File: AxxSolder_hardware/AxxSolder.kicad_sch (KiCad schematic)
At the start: 152 parts, among them IC1 TLV76733DRVR, IC2 OPA2387DSGT, IC3 LMR54406DBVR, IC4 STM32G431CBT6, IC5 TPD4E1U06DBVR, IC6 STUSB4500QTR, IC7 MAX16171ATA_VY+T, IC8 LTC4440AHMS8E, IC9 INA281A5QDBVRQ1, J1 USB4110-GF-A, J2 691243110009, J3 TSW-102-07-T-S, J4 61300611821, J5 TSW-102-07-T-S, J6 TSW-102-07-T-S, J7 TSW-108-07-T-S, J8 Conn_01x01_Pin, Q1 STL9P3LLH6, Q2 STL10N3LLH5, Q3 2N7002NXAKR, U2 PEC11J-9215F-S0015, U3 BSC014N04LS

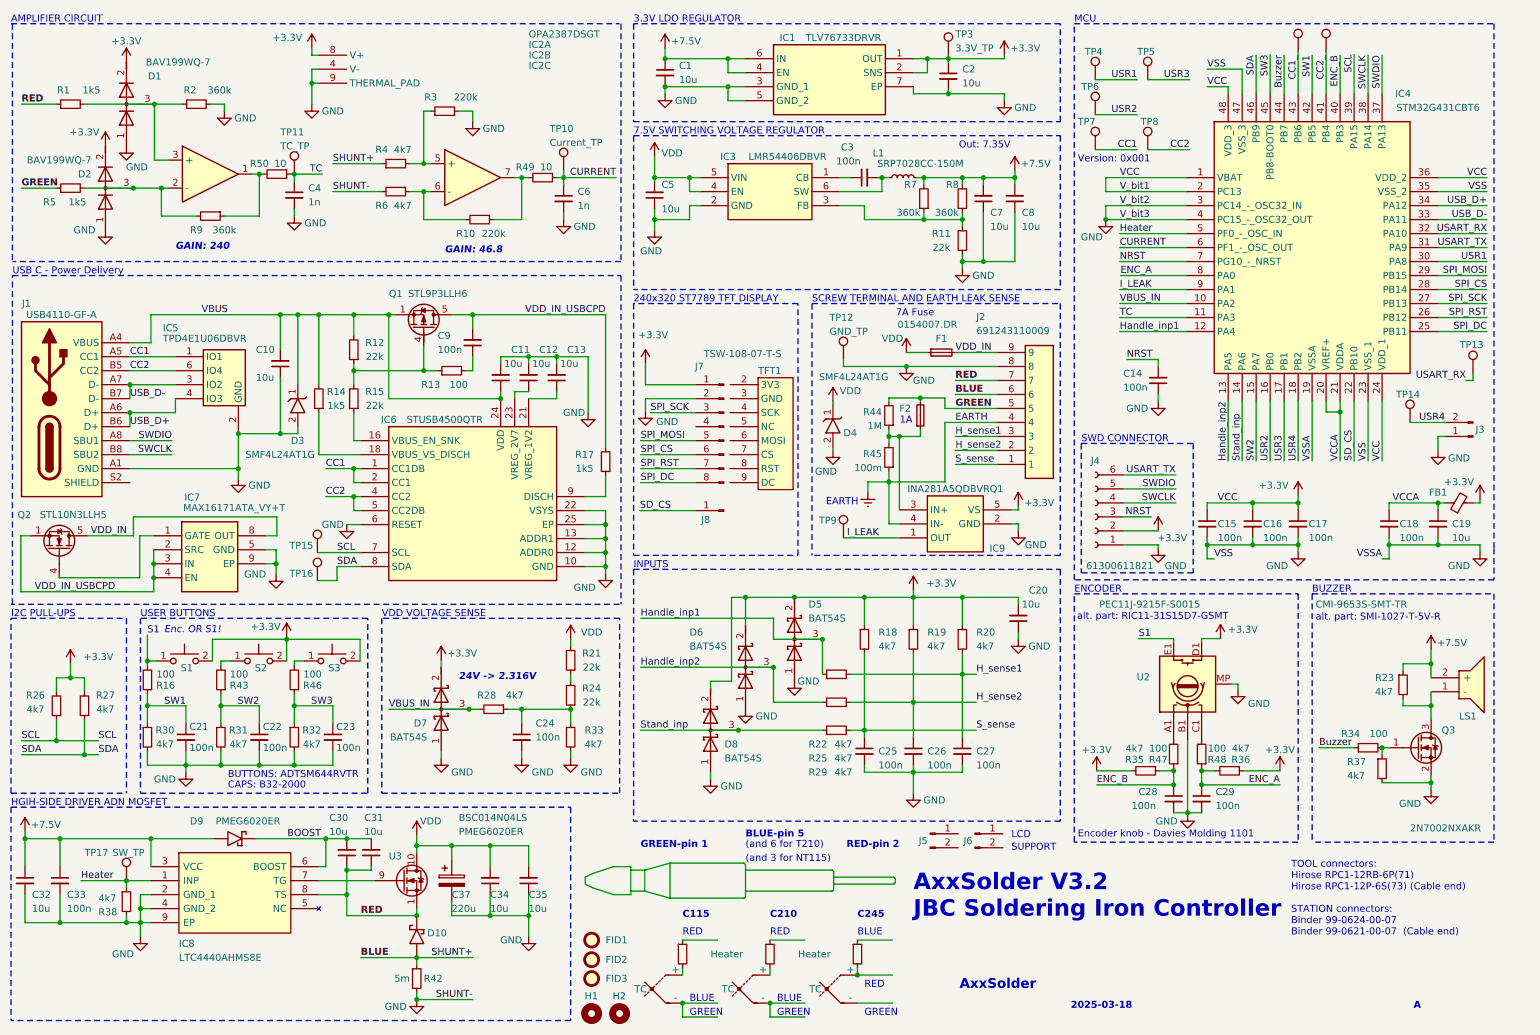
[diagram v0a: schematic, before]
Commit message: added pwr connections for relay add on board
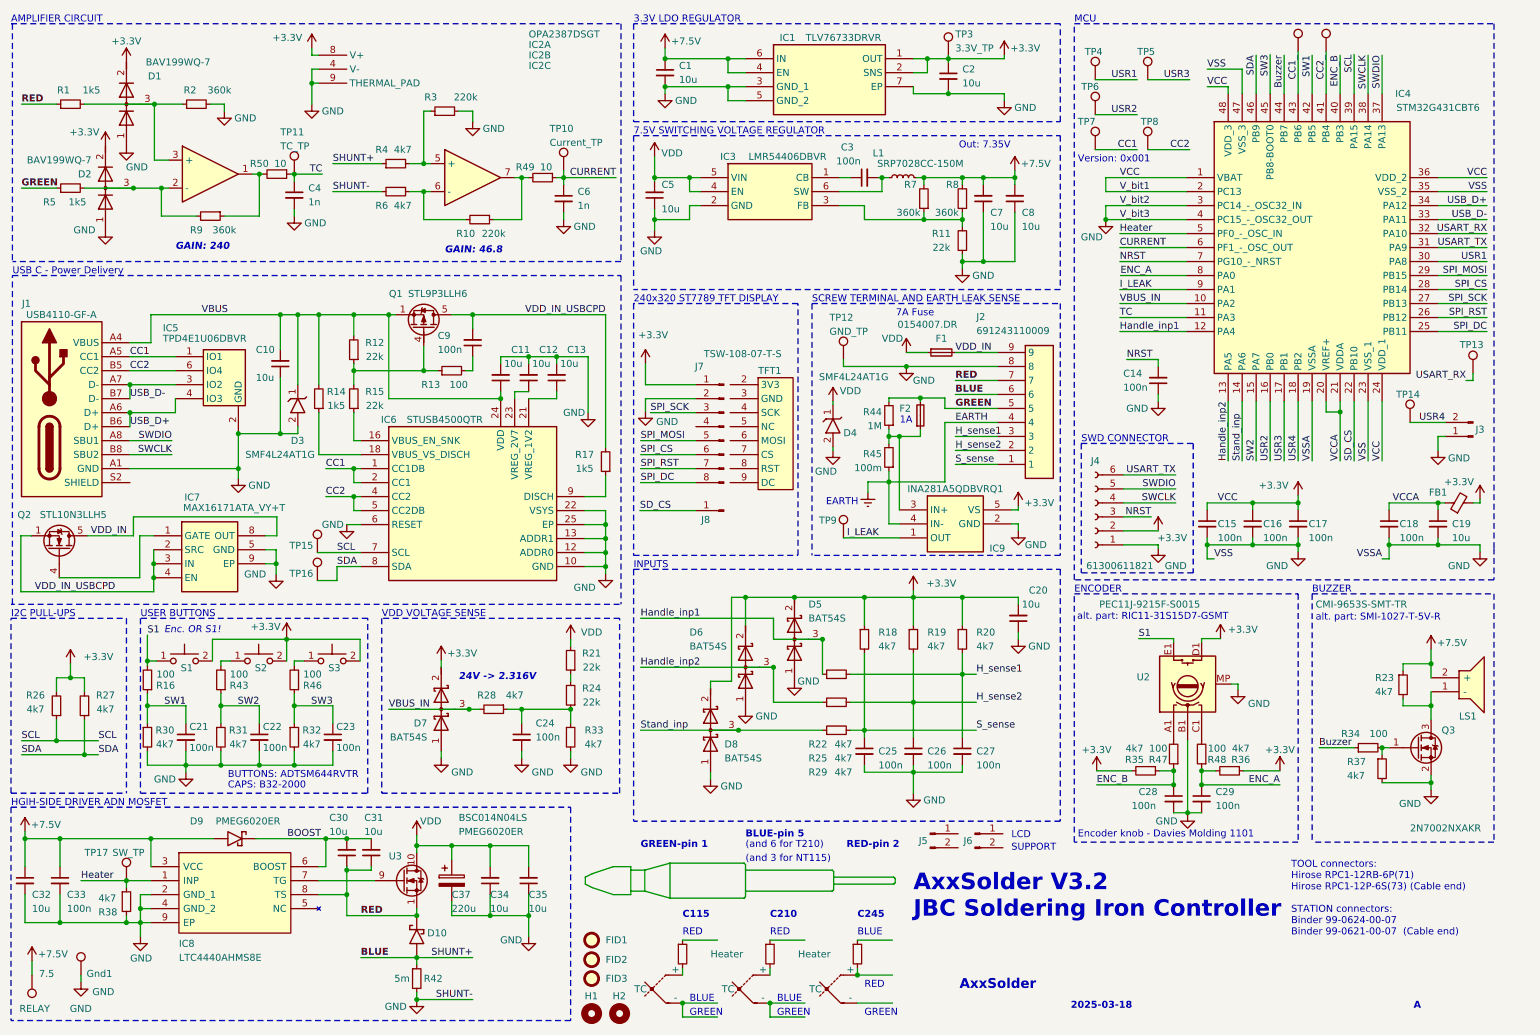
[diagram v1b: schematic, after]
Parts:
- added 7.5: RELAY, TestPoint:TestPoint_Keystone_5019_Miniature, symbol Connector:TestPoint
- added Gnd1: GND, TestPoint:TestPoint_Keystone_5019_Miniature, symbol Connector:TestPoint
- C37: footprint CAPAE830X1050N -> footprints:CAPAE830X1050N
- IC3, IC5: footprint SOT95P280X145-6N -> footprints:SOT95P280X145-6N
- J1: footprint USB4110GFA -> footprints:USB4110GFA
- J7: footprint TSW-108-XX-YY-S -> footprints:TSW-108-XX-YY-S
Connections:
- net +7.5V: now also 7.5.1
- net GND: now also Gnd1.1

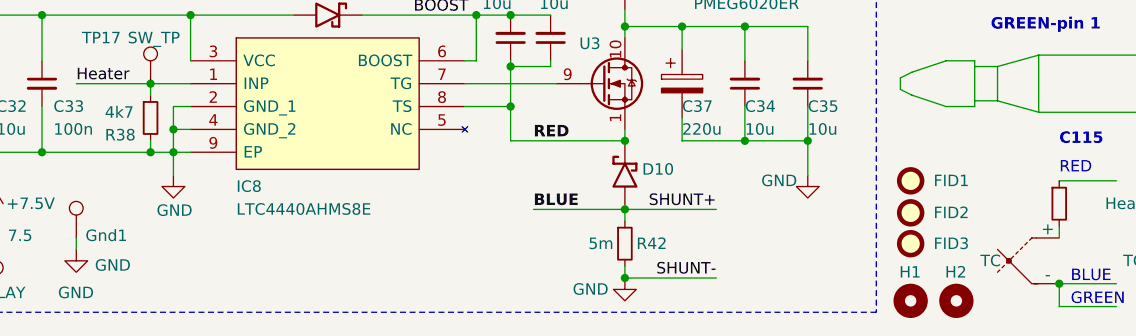
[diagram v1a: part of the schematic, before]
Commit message: enlarged PCB
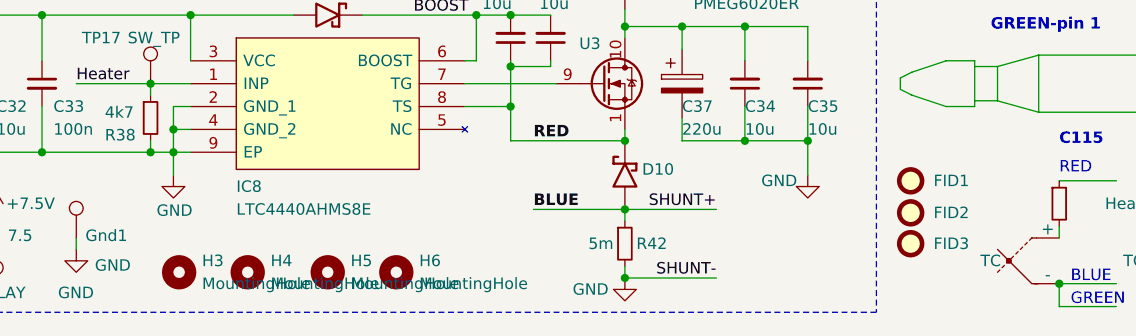
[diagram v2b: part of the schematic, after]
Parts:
- removed H1, H2: MountingHole, MountingHole:MountingHole_2.5mm, symbol Mechanical:MountingHole
- added H3, H4, H5, H6: MountingHole, MountingHole:MountingHole_3.2mm_M3, symbol Mechanical:MountingHole
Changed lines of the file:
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@@
 	)
 	(symbol
+		(lib_name "MountingHole_3")
+		(lib_id "Mechanical:MountingHole")
+		(at 54.61 191.77 0)
+		(unit 1)
+		(exclude_from_sim yes)
+		(in_bom no)
+		(on_board yes)
+		(dnp no)
+		(fields_autoplaced yes)
+		(property "Reference" "H5"
+			(at 57.15 190.4999 0)
+			(effects
+				(font
+					(size 1.27 1.27)
+				)
+				(justify left)
+			)
+		)
+		(property "Value" "MountingHole"
+			(at 57.15 193.0399 0)
+			(effects
+				(font
+					(size 1.27 1.27)
+				)
+				(justify left)
+			)
+		)
+		(property "Footprint" "MountingHole:MountingHole_3.2mm_M3"
+			(at 54.61 191.77 0)
+			(effects
+				(font
+					(size 1.27 1.27)
+				)
+				(hide yes)
+			)
+		)
+		(property "Datasheet" "~"
+			(at 54.61 191.77 0)
+			(effects
+				(font
+					(size 1.27 1.27)
+				)
+				(hide yes)
+			)
+		)
+		(property "Description" "Mounting Hole without connection"
+			(at 54.61 191.77 0)
+			(effects
+				(font
+					(size 1.27 1.27)
+				)
+				(hide yes)
+			)
+		)
+		(instances
+			(project ""
+				(path "/d71363c3-4d90-469c-a600-831e2a7cdaef"
+					(reference "H5")
+					(unit 1)
+				)
+			)
+		)
+	)
+	(symbol
 		(lib_id "Device:R_Small")
 		(at 235.204 150.876 270)
@@
 	)
 	(symbol
-		(lib_id "Mechanical:MountingHole")
-		(at 119.38 194.945 0)
-		(unit 1)
-		(exclude_from_sim no)
-		(in_bom no)
-		(on_board yes)
-		(dnp no)
-		(property "Reference" "H1"
-			(at 118.11 191.77 0)
-			(effects
-				(font
-					(size 1.27 1.27)
-				)
-				(justify left)
-			)
-		)
-		(property "Value" "MountingHole"
-			(at 121.92 196.2149 0)
-			(effects
-				(font
-					(size 1.27 1.27)
-				)
-				(justify left)
-				(hide yes)
-			)
-		)
-		(property "Footprint" "MountingHole:MountingHole_2.5mm"
-			(at 119.38 194.945 0)
-			(effects
-				(font
-					(size 1.27 1.27)
-				)
-				(hide yes)
-			)
-		)
-		(property "Datasheet" "~"
-			(at 119.38 194.945 0)
-			(effects
-				(font
-					(size 1.27 1.27)
-				)
-				(hide yes)
-			)
-		)
-		(property "Description" ""
-			(at 119.38 194.945 0)
-			(effects
-				(font
-					(size 1.27 1.27)
-				)
-			)
-		)
-		(property "Assembly Comment" "N/A"
-			(at 119.38 194.945 0)
-			(effects
-				(font
-					(size 1.27 1.27)
-				)
-				(hide yes)
-			)
-		)
-		(property "Manufacturing comment" "Do Not Place"
-			(at 119.38 194.945 0)
-			(effects
-				(font
-					(size 1.27 1.27)
-				)
-				(hide yes)
-			)
-		)
-		(instances
-			(project "AxxSolder"
-				(path "/d71363c3-4d90-469c-a600-831e2a7cdaef"
-					(reference "H1")
-					(unit 1)
-				)
-			)
-		)
-	)
-	(symbol
 		(lib_id "power:GND")
 		(at 176.53 77.47 0)
@@
 	)
 	(symbol
+		(lib_name "MountingHole_4")
+		(lib_id "Mechanical:MountingHole")
+		(at 62.23 191.77 0)
+		(unit 1)
+		(exclude_from_sim yes)
+		(in_bom no)
+		(on_board yes)
+		(dnp no)
+		(fields_autoplaced yes)
+		(property "Reference" "H6"
+			(at 64.77 190.4999 0)
+			(effects
+				(font
+					(size 1.27 1.27)
+				)
+				(justify left)
+			)
+		)
+		(property "Value" "MountingHole"
+			(at 64.77 193.0399 0)
+			(effects
+				(font
+					(size 1.27 1.27)
+				)
+				(justify left)
+			)
+		)
+		(property "Footprint" "MountingHole:MountingHole_3.2mm_M3"
+			(at 62.23 191.77 0)
+			(effects
+				(font
+					(size 1.27 1.27)
+				)
+				(hide yes)
+			)
+		)
+		(property "Datasheet" "~"
+			(at 62.23 191.77 0)
+			(effects
+				(font
+					(size 1.27 1.27)
+				)
+				(hide yes)
+			)
+		)
+		(property "Description" "Mounting Hole without connection"
+			(at 62.23 191.77 0)
+			(effects
+				(font
+					(size 1.27 1.27)
+				)
+				(hide yes)
+			)
+		)
+		(instances
+			(project ""
+				(path "/d71363c3-4d90-469c-a600-831e2a7cdaef"
+					(reference "H6")
+					(unit 1)
+				)
+			)
+		)
+	)
+	(symbol
 		(lib_id "Connector:TestPoint")
 		(at 26.67 187.96 0)
@@
 	)
 	(symbol
+		(lib_name "MountingHole_2")
+		(lib_id "Mechanical:MountingHole")
+		(at 45.72 191.77 0)
+		(unit 1)
+		(exclude_from_sim yes)
+		(in_bom no)
+		(on_board yes)
+		(dnp no)
+		(fields_autoplaced yes)
+		(property "Reference" "H4"
+			(at 48.26 190.4999 0)
+			(effects
+				(font
+					(size 1.27 1.27)
+				)
+				(justify left)
+			)
+		)
+		(property "Value" "MountingHole"
+			(at 48.26 193.0399 0)
+			(effects
+				(font
+					(size 1.27 1.27)
+				)
+				(justify left)
+			)
+		)
+		(property "Footprint" "MountingHole:MountingHole_3.2mm_M3"
+			(at 45.72 191.77 0)
+			(effects
+				(font
+					(size 1.27 1.27)
+				)
+				(hide yes)
+			)
+		)
+		(property "Datasheet" "~"
+			(at 45.72 191.77 0)
+			(effects
+				(font
+					(size 1.27 1.27)
+				)
+				(hide yes)
+			)
+		)
+		(property "Description" "Mounting Hole without connection"
+			(at 45.72 191.77 0)
+			(effects
+				(font
+					(size 1.27 1.27)
+				)
+				(hide yes)
+			)
+		)
+		(instances
+			(project ""
+				(path "/d71363c3-4d90-469c-a600-831e2a7cdaef"
+					(reference "H4")
+					(unit 1)
+				)
+			)
+		)
+	)
+	(symbol
 		(lib_id "Device:C_Small")
 		(at 65.405 46.355 0)
@@
 	)
 	(symbol
-		(lib_id "Mechanical:MountingHole")
-		(at 124.46 194.945 0)
-		(unit 1)
-		(exclude_from_sim no)
-		(in_bom no)
-		(on_board yes)
-		(dnp no)
-		(property "Reference" "H2"
-			(at 123.19 191.77 0)
-			(effects
-				(font
-					(size 1.27 1.27)
-				)
-				(justify left)
-			)
-		)
-		(property "Value" "MountingHole"
-			(at 127 196.2149 0)
-			(effects
-				(font
-					(size 1.27 1.27)
-				)
-				(justify left)
-				(hide yes)
-			)
-		)
-		(property "Footprint" "MountingHole:MountingHole_2.5mm"
-			(at 124.46 194.945 0)
-			(effects
-				(font
-					(size 1.27 1.27)
-				)
-				(hide yes)
-			)
-		)
-		(property "Datasheet" "~"
-			(at 124.46 194.945 0)
-			(effects
-				(font
-					(size 1.27 1.27)
-				)
-				(hide yes)
-			)
-		)
-		(property "Description" ""
-			(at 124.46 194.945 0)
-			(effects
-				(font
-					(size 1.27 1.27)
-				)
-			)
-		)
-		(property "Assembly Comment" "N/A"
-			(at 124.46 194.945 0)
-			(effects
-				(font
-					(size 1.27 1.27)
-				)
-				(hide yes)
-			)
-		)
-		(property "Manufacturing comment" "Do Not Place"
-			(at 124.46 194.945 0)
-			(effects
-				(font
-					(size 1.27 1.27)
-				)
-				(hide yes)
-			)
-		)
-		(instances
-			(project "AxxSolder"
-				(path "/d71363c3-4d90-469c-a600-831e2a7cdaef"
-					(reference "H2")
-					(unit 1)
-				)
-			)
-		)
-	)
-	(symbol
 		(lib_id "power:GND")
 		(at 97.79 33.02 0)
@@
 					(unit 1)
 				)
+			)
+		)
+	)
+	(symbol
+		(lib_name "MountingHole_1")
+		(lib_id "Mechanical:MountingHole")
+		(at 38.1 191.77 0)
+		(unit 1)
+		(exclude_from_sim yes)
+		(in_bom no)
+		(on_board yes)
+		(dnp no)
+		(fields_autoplaced yes)
+		(property "Reference" "H3"
+			(at 40.64 190.4999 0)
+			(effects
+				(font
+					(size 1.27 1.27)
+				)
+				(justify left)
+			)
+		)
+		(property "Value" "MountingHole"
+			(at 40.64 193.0399 0)
+			(effects
+				(font
+					(size 1.27 1.27)
+				)
+				(justify left)
+			)
+		)
+		(property "Footprint" "MountingHole:MountingHole_3.2mm_M3"
+			(at 38.1 191.77 0)
+			(effects
+				(font
+					(size 1.27 1.27)
+				)
+				(hide yes)
+			)
+		)
+		(property "Datasheet" "~"
+			(at 38.1 191.77 0)
+			(effects
+				(font
+					(size 1.27 1.27)
+				)
+				(hide yes)
+			)
+		)
+		(property "Description" "Mounting Hole without connection"
+			(at 38.1 191.77 0)
+			(effects
+				(font
+					(size 1.27 1.27)
+				)
+				(hide yes)
+			)
+		)
+		(instances
+			(project ""
+				(path "/d71363c3-4d90-469c-a600-831e2a7cdaef"
+					(reference "H3")
+					(unit 1)
+				)
